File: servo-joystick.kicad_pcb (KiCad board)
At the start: 2 copper layers, 100 x 80 mm, 105 parts, among them P1 CONN_01X02, P2 CONN_01X03, P3 CONN_01X03, P4 CONN_01X03, P5 CONN_01X03, U1 MCP6002, U2 MCP6004, U3 MCP6004, U4 MCP6004, U5 SN74LVC1G3157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

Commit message: Rev A
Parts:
- added TP4: CTRL1, olof:TEST_POINT_THD_NO_CIRC, F.Cu at (96.2, 142.5)
- added TP5: INT1, olof:TEST_POINT_THD_NO_CIRC, F.Cu at (78.8, 141.5)
- added TP6: SAW, olof:TEST_POINT_THD_NO_CIRC, F.Cu at (83.8, 91.2)
- added TP7: BUF1, olof:TEST_POINT_THD_NO_CIRC, F.Cu at (101.2, 97.5)
- added TP8: PWM1, olof:TEST_POINT_THD_NO_CIRC, F.Cu at (101.2, 91.2)
- R10, R18, R26, R34: value 43k -> 62k
- R11, R19, R27, R35: value 24k -> 11k
- R12, R13, R20, R21, R28, R29, R36, R37: value 150k -> 100k
- R14, R22, R30, R38: value 680 -> 470
- R16, R24, R32, R8: value 24k -> 270k
- R17, R25, R33, R9: value 680 -> 3k9
- RV1, RV2, RV3, RV4, RV5, RV6, RV7, RV8: value 10k -> 1k
- moved R24 49.7 mm to (68.8, 145.1), turned to 270 degrees
- moved R8 49.6 mm to (81.2, 145.0), turned to 270 degrees
- moved R9 43.1 mm to (87.4, 142.5), turned to 180 degrees
- moved R25 41.9 mm to (59.9, 142.4), turned to 180 degrees
- moved R17 25.0 mm to (96.2, 123.8)
- moved R33 25.0 mm to (53.8, 123.8)
- moved R32 23.0 mm to (69.9, 126.8), turned to 180 degrees
- moved R16 23.0 mm to (79.9, 126.8), turned to 0 degrees
- moved C3 4.88 mm to (33.6, 106.8), turned to 90 degrees
- moved P1 3.31 mm to (28.4, 111.8), turned to 0 degrees
- moved R19 2.50 mm to (90.0, 112.5)
- moved R18 2.50 mm to (92.5, 112.6)
- moved R34 2.50 mm to (57.5, 112.5)
- moved R35 2.50 mm to (60.0, 112.5)
- moved RV1 2.50 mm to (88.8, 148.8), turned to 90 degrees
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- renumbered W1 to TP1, W2 to TP2, W3 to TP3
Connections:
- net /PWM #1/BUF_OUT renamed /PWM #1/BUF
- net /PWM #2/BUF_OUT renamed /PWM #2/BUF
- net /PWM #3/BUF_OUT renamed /PWM #3/BUF
- net /PWM #4/BUF_OUT renamed /PWM #4/BUF
- R10 pad 1: /PWM #1/VREF_ADJ -> VCC
- R10 pad 2: /PWM #1/VREF -> /PWM #1/VREF_ADJ_P
- R11 pad 1: /PWM #1/VREF -> /PWM #1/VREF_ADJ_M
- R16 pad 1: /PWM #2/VIN_ADJ -> /PWM #2/VIN
- R16 pad 2: /PWM #2/VIN_DIV -> /PWM #2/VIN_ADJ_P
- R17 pad 1: /PWM #2/VIN_DIV -> /PWM #2/VIN_ADJ_M
- R18 pad 1: /PWM #2/VREF_ADJ -> VCC
- R18 pad 2: /PWM #2/VREF -> /PWM #2/VREF_ADJ_P
- R19 pad 1: /PWM #2/VREF -> /PWM #2/VREF_ADJ_M
- R24 pad 1: /PWM #3/VIN_ADJ -> /PWM #3/VIN
- R24 pad 2: /PWM #3/VIN_DIV -> /PWM #3/VIN_ADJ_P
- R25 pad 1: /PWM #3/VIN_DIV -> /PWM #3/VIN_ADJ_M
- R26 pad 1: /PWM #3/VREF_ADJ -> VCC
- R26 pad 2: /PWM #3/VREF -> /PWM #3/VREF_ADJ_P
- R27 pad 1: /PWM #3/VREF -> /PWM #3/VREF_ADJ_M
- R32 pad 1: /PWM #4/VIN_ADJ -> /PWM #4/VIN
- R32 pad 2: /PWM #4/VIN_DIV -> /PWM #4/VIN_ADJ_P
- R33 pad 1: /PWM #4/VIN_DIV -> /PWM #4/VIN_ADJ_M
- R34 pad 1: /PWM #4/VREF_ADJ -> VCC
- R34 pad 2: /PWM #4/VREF -> /PWM #4/VREF_ADJ_P
- R35 pad 1: /PWM #4/VREF -> /PWM #4/VREF_ADJ_M
- R8 pad 1: /PWM #1/VIN_ADJ -> /PWM #1/VIN
- R8 pad 2: /PWM #1/VIN_DIV -> /PWM #1/VIN_ADJ_P
- R9 pad 1: /PWM #1/VIN_DIV -> /PWM #1/VIN_ADJ_M
- RV1 pad 1: /PWM #1/VIN -> /PWM #1/VIN_ADJ_P
- RV1 pad 2: /PWM #1/VIN -> /PWM #1/VIN_DIV
- RV1 pad 3: /PWM #1/VIN_ADJ -> /PWM #1/VIN_ADJ_M
- RV2 pad 1: VCC -> /PWM #1/VREF_ADJ_P
- RV2 pad 2: VCC -> /PWM #1/VREF
- RV2 pad 3: /PWM #1/VREF_ADJ -> /PWM #1/VREF_ADJ_M
- RV3 pad 1: /PWM #2/VIN -> /PWM #2/VIN_ADJ_P
- RV3 pad 2: /PWM #2/VIN -> /PWM #2/VIN_DIV
- RV3 pad 3: /PWM #2/VIN_ADJ -> /PWM #2/VIN_ADJ_M
- RV4 pad 1: VCC -> /PWM #2/VREF_ADJ_P
- RV4 pad 2: VCC -> /PWM #2/VREF
- RV4 pad 3: /PWM #2/VREF_ADJ -> /PWM #2/VREF_ADJ_M
- RV5 pad 1: /PWM #3/VIN -> /PWM #3/VIN_ADJ_P
- RV5 pad 2: /PWM #3/VIN -> /PWM #3/VIN_DIV
- RV5 pad 3: /PWM #3/VIN_ADJ -> /PWM #3/VIN_ADJ_M
- RV6 pad 1: VCC -> /PWM #3/VREF_ADJ_P
- RV6 pad 2: VCC -> /PWM #3/VREF
- RV6 pad 3: /PWM #3/VREF_ADJ -> /PWM #3/VREF_ADJ_M
- RV7 pad 1: /PWM #4/VIN -> /PWM #4/VIN_ADJ_P
- RV7 pad 2: /PWM #4/VIN -> /PWM #4/VIN_DIV
- RV7 pad 3: /PWM #4/VIN_ADJ -> /PWM #4/VIN_ADJ_M
- RV8 pad 1: VCC -> /PWM #4/VREF_ADJ_P
- RV8 pad 2: VCC -> /PWM #4/VREF
- RV8 pad 3: /PWM #4/VREF_ADJ -> /PWM #4/VREF_ADJ_M
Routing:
- net GND: track 58.6 -> 602.9 mm
- net VCC: track 230.0 -> 586.3 mm
- net /PWM #1/VIN_ADJ: track 63.9 -> 0.00 mm, vias 2 -> 0
- net /PWM #1/VIN_DIV: track 5.12 -> 68.2 mm
- net /PWM #3/VIN_DIV: track 5.00 -> 67.5 mm, vias 0 -> 2
- net /PWM #3/VIN_ADJ: track 55.7 -> 0.00 mm, vias 2 -> 0
- net /PWM #2/VIN_ADJ: track 41.0 -> 0.00 mm
- net /PWM #2/VIN_DIV: track 5.00 -> 35.5 mm
- net /PWM #4/VIN_DIV: track 5.00 -> 30.4 mm
- net /PWM #4/VIN_ADJ: track 25.0 -> 0.00 mm, vias 1 -> 0
- net /PWM #2/VREF_ADJ_P: track 0.00 -> 18.0 mm
- net /PWM #3/VREF: track 8.46 -> 26.2 mm
- net /PWM #3/VREF_ADJ_M: track 0.00 -> 15.6 mm
- net /PWM #2/VREF_ADJ_M: track 0.00 -> 15.4 mm
- net /PWM #3/VIN: track 27.7 -> 14.2 mm
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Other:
- board text added: "2017-12-09"
- board text added: "Dual joystick servo controller"
- board text removed: "2017-11-15"
- board text removed: "Dual joystick"
- board text removed: "servo controller"

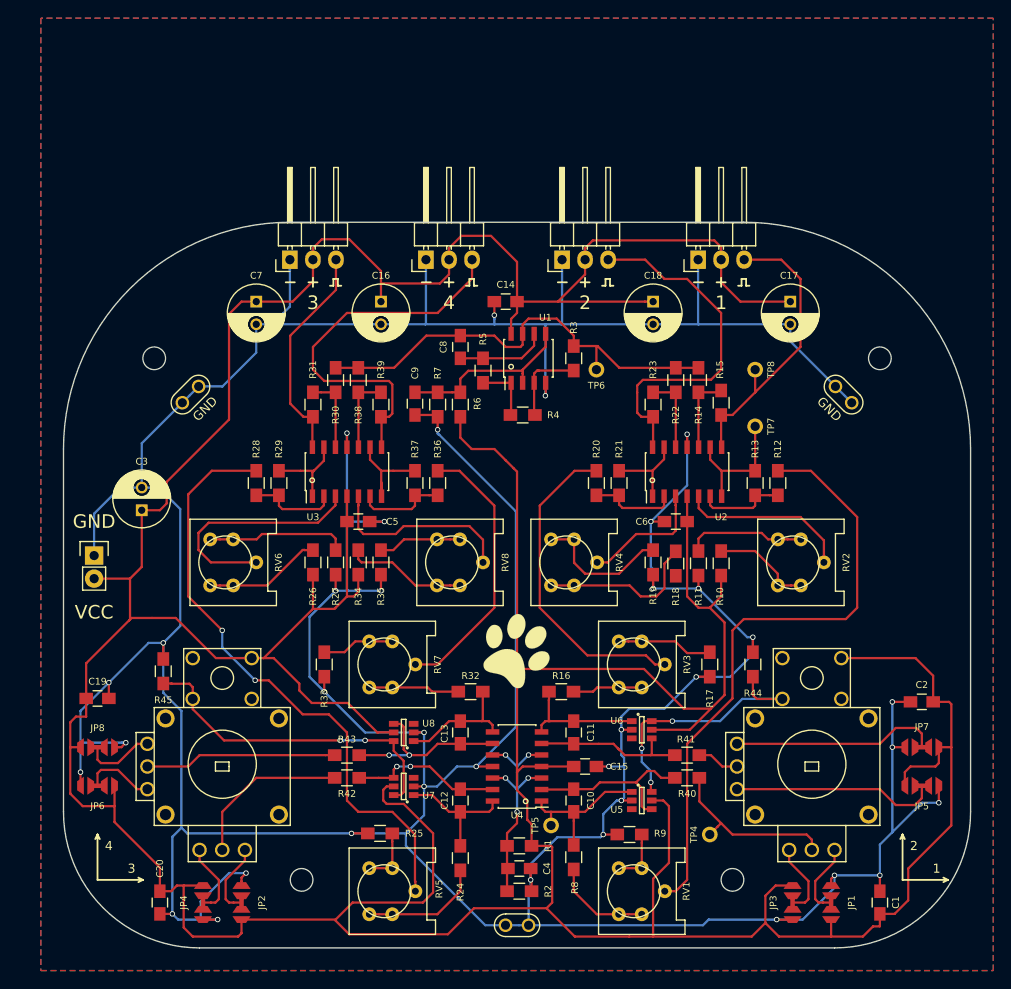
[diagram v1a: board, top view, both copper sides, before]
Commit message: Removed 0R resistors and started new layout
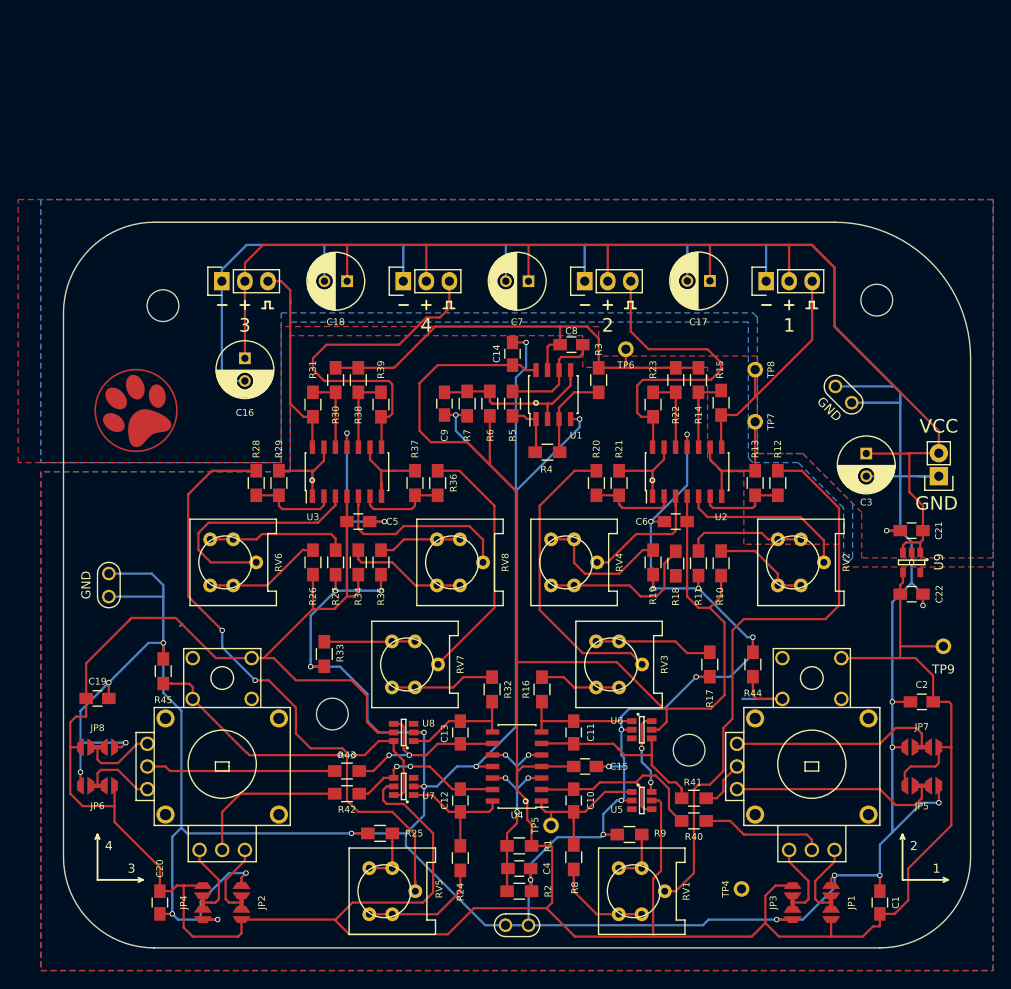
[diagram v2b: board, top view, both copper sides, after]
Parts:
- removed the G*** at (74.9, 122.1)
- added C21: 2u2, olof:C_0805_HandSoldering, F.Cu at (118.5, 109.0)
- added C22: 2u2, olof:C_0805_HandSoldering, F.Cu at (118.5, 116.0)
- added G***: LOGO, Logo:paw-large-cu-circ, F.Cu at (33.0, 95.8)
- added TP9: VCC, olof:TEST_POINT_THD_NO_CIRC, F.Cu at (122.0, 121.8)
- added U9: LD2981, TO_SOT_Packages_SMD:SOT-23-5, F.Cu at (118.5, 112.5)
- C10, C11, C12, C13: value 220n -> 100n
- MH6 (x4): footprint Mounting_Holes:MountingHole_2-5mm -> olof:MH-M3
- P2, P3, P4, P5: footprint Pin_Headers:Pin_Header_Angled_1x03 -> Pin_Headers:Pin_Header_Straight_1x03
- R10, R18, R26, R34: value 62k -> 30k
- R11, R19, R27, R35: value 11k -> 15k
- R12, R13, R20, R21, R28, R29, R36, R37: value 100k -> 150k
- R16, R24, R32, R8: value 270k -> 30k
- R17, R25, R33, R9: value 3k9 -> 470
- RV1, RV3, RV5, RV7: value 1k -> 100
- moved P1 93.5 mm to (121.5, 103.0), turned to 180 degrees
- moved C3 80.1 mm to (113.5, 100.5), turned to 270 degrees
- moved C18 33.8 mm to (56.3, 81.5), turned to 180 degrees
- moved C7 30.1 mm to (76.3, 81.5), turned to 180 degrees
- moved TP1 22.8 mm to (30.0, 115.0), turned to 90 degrees
- moved MH6 18.6 mm to (54.6, 129.2)
- moved C16 16.2 mm to (45.0, 90.0)
- moved MH6 15.1 mm to (94.0, 133.2)
- moved C8 12.3 mm to (81.0, 88.5), turned to 0 degrees
- moved C17 9.14 mm to (96.3, 81.5), turned to 180 degrees
- moved P2 7.87 mm to (102.5, 81.5)
- moved P4 7.87 mm to (42.5, 81.5)
- moved TP4 6.95 mm to (99.8, 148.5)
- moved MH6 6.42 mm to (114.7, 83.6)
- moved MH6 5.88 mm to (36.0, 84.2)
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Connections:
- C16 pad 1: VCC -> +6V
- C17 pad 1: VCC -> +6V
- C18 pad 1: VCC -> +6V
- C3 pad 1: VCC -> +6V
- C7 pad 1: VCC -> +6V
- P1 pad 2: VCC -> +6V
- P2 pad 2: VCC -> +6V
- P3 pad 2: VCC -> +6V
- P4 pad 2: VCC -> +6V
- P5 pad 2: VCC -> +6V
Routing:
- net +6V: track 0.00 -> 149.1 mm
- net VCC: track 586.3 -> 474.0 mm
- net GND: track 602.9 -> 673.6 mm, vias 36 -> 39
- net /Integrator #1/SW: track 30.0 -> 19.0 mm, vias 3 -> 2
- net /PWM #1/PWM: track 32.5 -> 26.5 mm
- net /Integrator #1/VIN: track 19.6 -> 13.6 mm
- net /PWM #1/SAWTOOTH: track 50.1 -> 54.6 mm
- net /PWM #4/PWM: track 42.7 -> 38.5 mm
- net /Integrator #2/INT_FB: track 17.4 -> 21.4 mm
- net /Integrator #1/INT_FB: track 20.0 -> 23.6 mm
- net /PWM #2/PWM: track 39.7 -> 36.2 mm
- net /PWM #1/VIN_DIV: track 68.2 -> 65.4 mm
- net /PWM #2/VIN_ADJ_M: track 10.7 -> 13.2 mm
- net /PWM #4/VIN_DIV: track 30.4 -> 27.9 mm
- net /PWM #2/VIN_DIV: track 35.5 -> 33.1 mm
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- added copper zone on F.Cu, net +6V
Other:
- outline, holes or cut-outs redrawn
- board text added: "2018-06-13"
- board text added: "Rev B"
- board text removed: "2017-12-09"
- board text removed: "Rev A"

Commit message: Larger SOT-23-6 pads
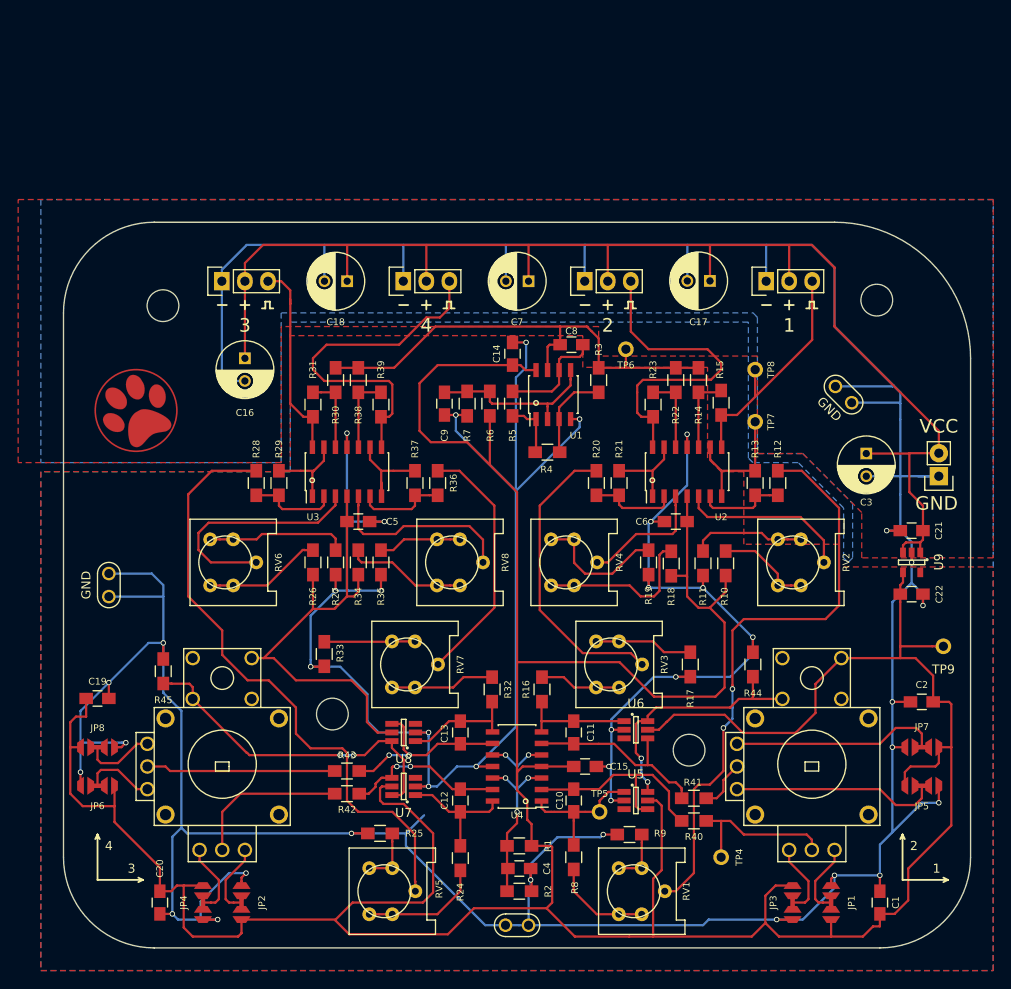
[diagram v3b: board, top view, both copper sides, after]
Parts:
- U5, U6, U7, U8: footprint TO_SOT_Packages_SMD:SOT-23-6 -> olof:SOT-23-6-Handsoldering
- moved TP5 5.56 mm to (84.1, 140.0)
- moved TP4 4.16 mm to (97.5, 145.0)
- moved R17 2.15 mm to (94.1, 123.8)
- moved U5 0.65 mm to (88.1, 138.8)
- moved U6 0.65 mm to (88.1, 130.9)
- moved R10 0.50 mm to (98.0, 112.6)
- moved R11 0.50 mm to (95.5, 112.6)
- moved R18 0.50 mm to (92.0, 112.6)
- moved R19 0.50 mm to (89.5, 112.5)
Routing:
- net /Integrator #1/SW: track 19.0 -> 28.3 mm
- net GND: track 673.6 -> 666.8 mm
- net /Integrator #1/VIN: track 13.6 -> 17.6 mm
- net /PWM #2/VIN_ADJ_M: track 13.2 -> 10.9 mm
- net /PWM #1/VIN: track 17.0 -> 15.3 mm
- net /PWM #2/VIN: track 13.3 -> 12.5 mm
- net /Integrator #1/INT_FB: track 23.6 -> 24.3 mm
- net /PWM #1/VREF_ADJ_M: track 13.2 -> 12.6 mm
- net /PWM #2/VREF_ADJ_M: track 15.4 -> 14.9 mm
- net /PWM #1/VREF_ADJ_P: track 11.1 -> 10.6 mm
- net /PWM #3/VIN_DIV: track 67.8 -> 68.3 mm, vias 2 -> 0
- net /PWM #1/VIN_DIV: vias 0 -> 2

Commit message: Larger SOT-23-5 pads
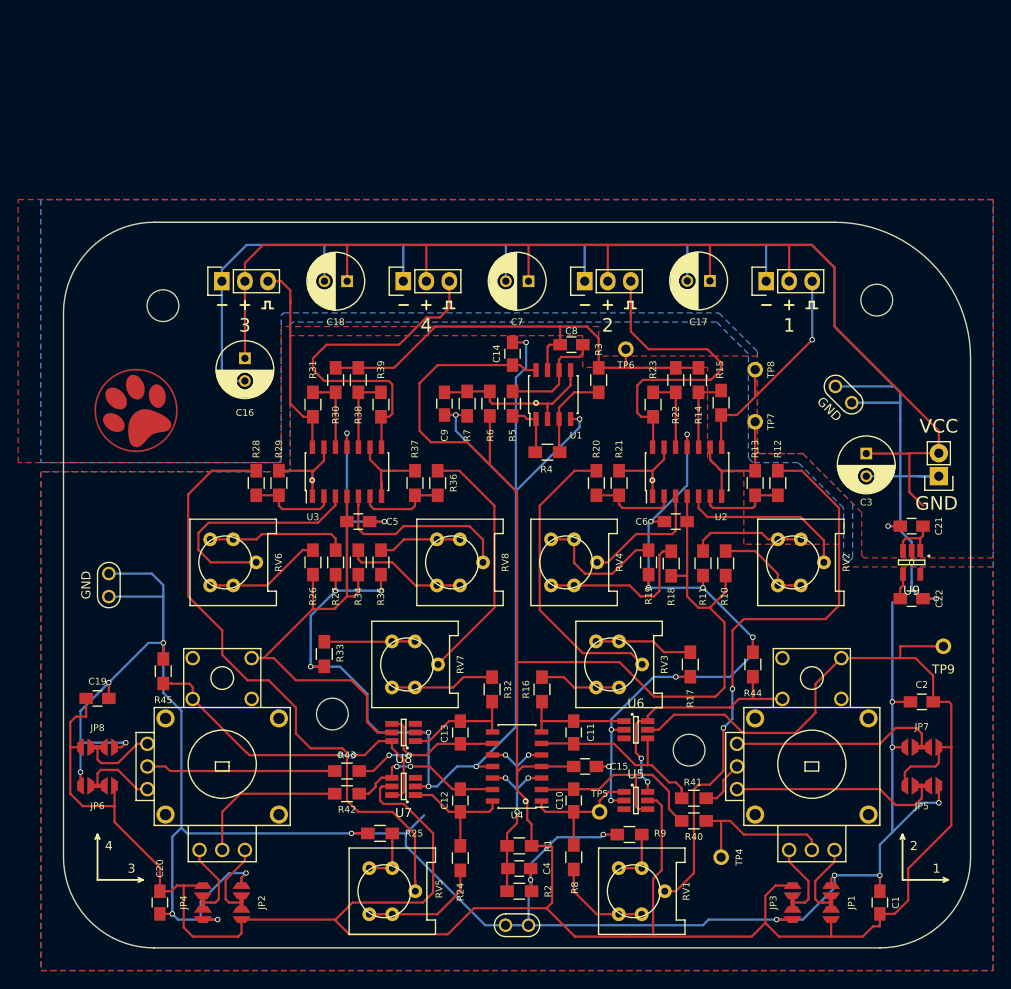
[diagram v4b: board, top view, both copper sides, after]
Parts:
- U9: footprint TO_SOT_Packages_SMD:SOT-23-5 -> olof:SOT-23-5-Handsoldering
- moved C21 0.50 mm to (118.5, 108.5)
- moved C22 0.50 mm to (118.5, 116.5)
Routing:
- net VCC: track 473.8 -> 468.3 mm
- net +6V: track 149.1 -> 146.9 mm
- net GND: track 666.8 -> 664.8 mm
- net /PWM #1/PWM: vias 0 -> 1

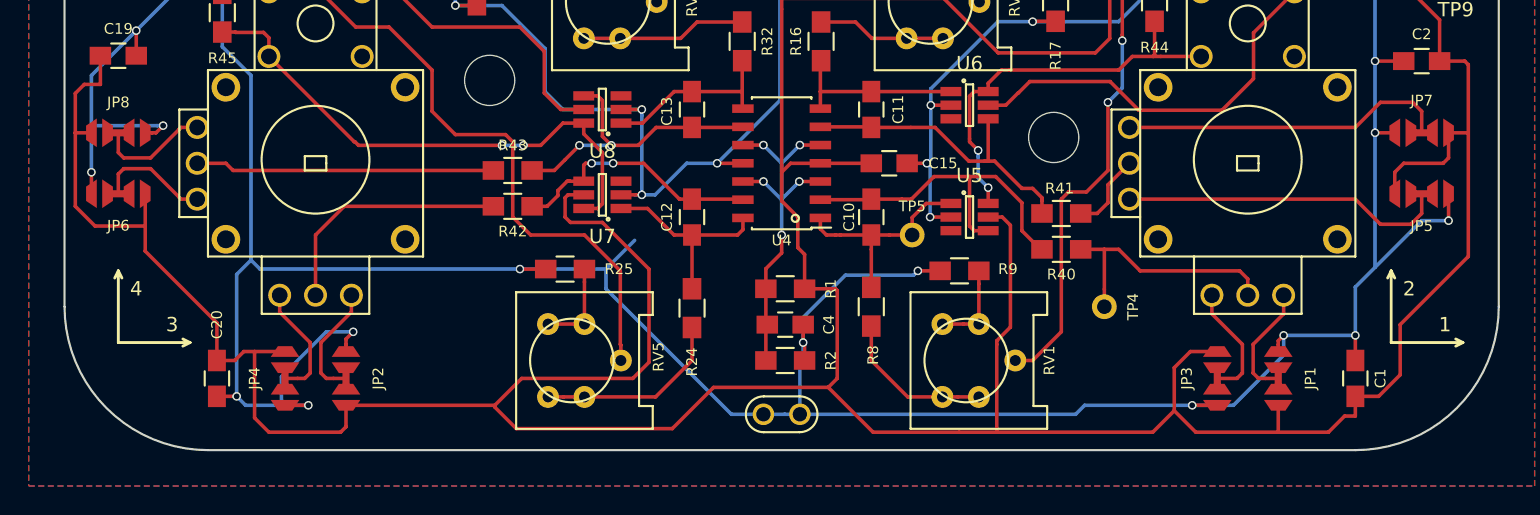
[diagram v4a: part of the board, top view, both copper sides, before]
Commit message: Better solder jumper footprint
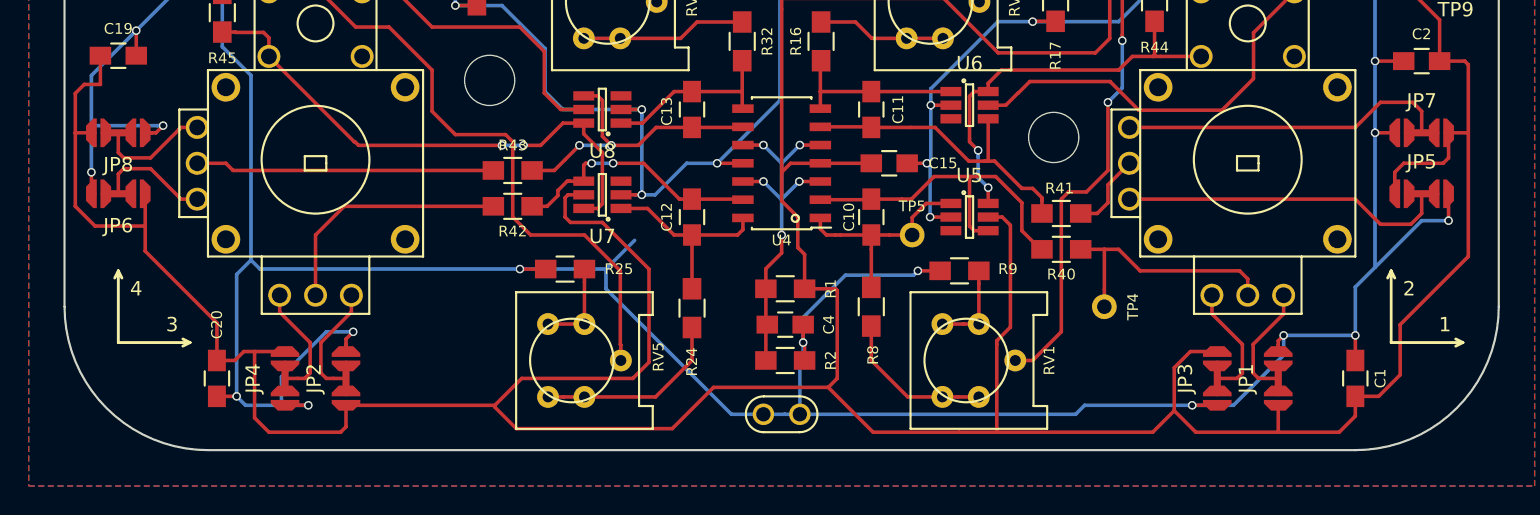
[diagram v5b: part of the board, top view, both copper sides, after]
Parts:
- moved G*** 2.50 mm to (75.0, 115.0)
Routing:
- net VCC: track 468.3 -> 471.3 mm
- net GND: track 664.8 -> 667.8 mm
- net Net-(JP8-Pad2): track 9.41 -> 10.2 mm
- net Net-(JP7-Pad2): track 24.4 -> 25.1 mm
- net Net-(JP6-Pad2): track 9.41 -> 10.2 mm
- net Net-(JP5-Pad2): track 24.3 -> 25.0 mm
- net Net-(JP4-Pad2): track 9.71 -> 10.5 mm
- net Net-(JP3-Pad2): track 9.71 -> 10.5 mm
- net Net-(JP2-Pad2): track 9.71 -> 10.5 mm
- net Net-(JP1-Pad2): track 9.71 -> 10.5 mm
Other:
- net class Default: clearance 0.25 -> 0.24
- rule trace_clearance: 0.25 -> 0.24
